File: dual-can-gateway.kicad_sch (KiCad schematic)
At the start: 96 parts, among them J3 Conn_01x02_Pin, Q1 AO3401A, Q2 2N7002, U1 STM32F405RGTx, U2 STM32F405RGTx, U3 ESP32-WROOM-32UE, U4 TJA1044GT-3, U5 TJA1044GT-3, U6 TJA1055T/3, U7 TJA1055T/3, U8 LM2596S-5, U9 AMS1117-3.3

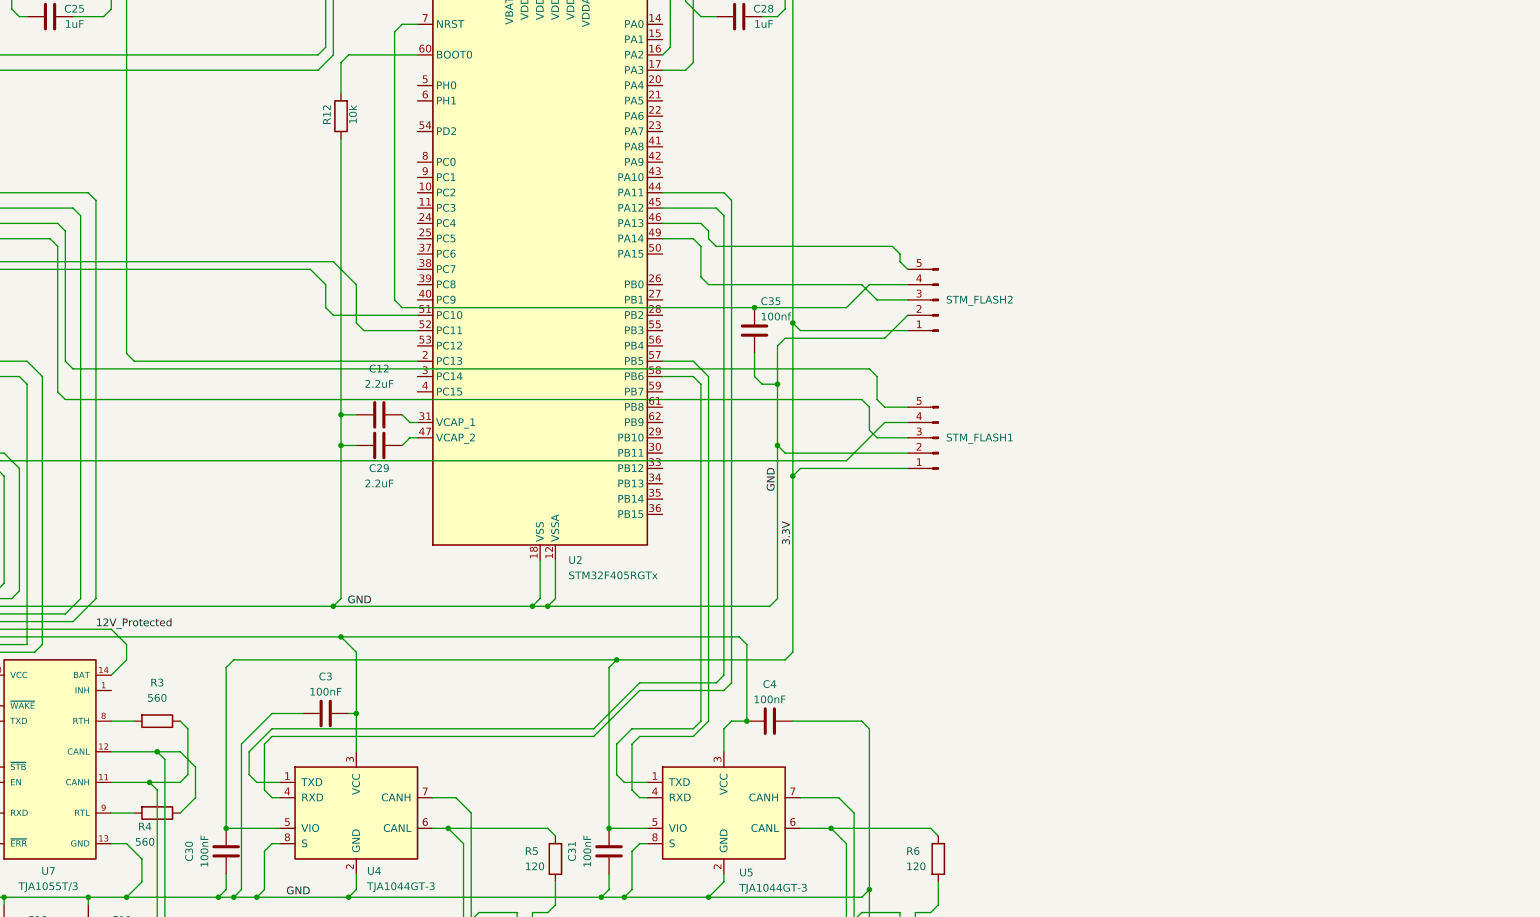
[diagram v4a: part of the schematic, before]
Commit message: added k-line
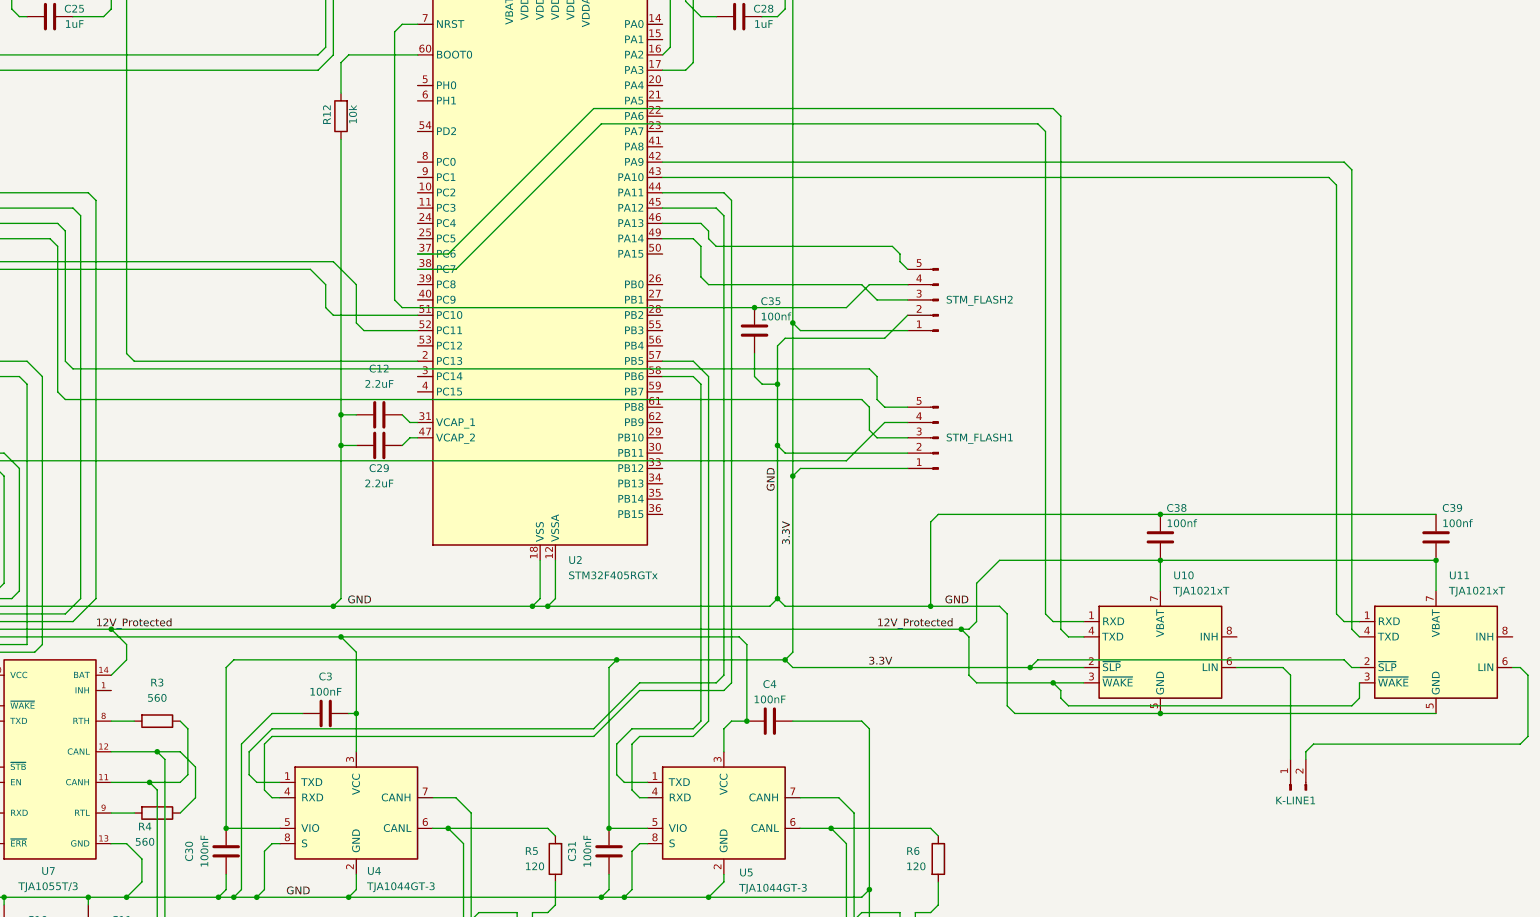
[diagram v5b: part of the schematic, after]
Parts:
- added C38, C39: 100nf, Capacitor_SMD:C_0805_2012Metric, symbol Device:C
- added K-LINE1: Conn_01x02_Pin, Connector_PinHeader_2.54mm:PinHeader_1x02_P2.54mm_Vertical, symbol Connector:Conn_01x02_Pin
- added U10, U11: TJA1021xT, Package_SO:SOIC-8_3.9x4.9mm_P1.27mm, symbol Interface_CAN_LIN:TJA1021xT
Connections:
- net 12V_Protected: now also C38.1, C39.1, U10.3 (~{WAKE}), U10.7 (VBAT), U11.3 (~{WAKE}), U11.7 (VBAT)
- net 3.3V: now also U10.2 (~{SLP}), U11.2 (~{SLP})
- net GND: now also C38.2, C39.2, U10.5 (GND), U11.5 (GND)
- net at U2.37 (PC6): now also U10.4 (TXD)
- net at U2.38 (PC7): now also U10.1 (RXD)
- net at U2.42 (PA9): now also U11.4 (TXD)
- net at U2.43 (PA10): now also U11.1 (RXD)
- new net: K-LINE1.2 (Pin_2), U11.6 (LIN)
- new net: K-LINE1.1 (Pin_1), U10.6 (LIN)
